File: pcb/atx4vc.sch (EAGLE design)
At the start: 38 parts, among them IC1 MY_7905DT, J2 ATX24RH

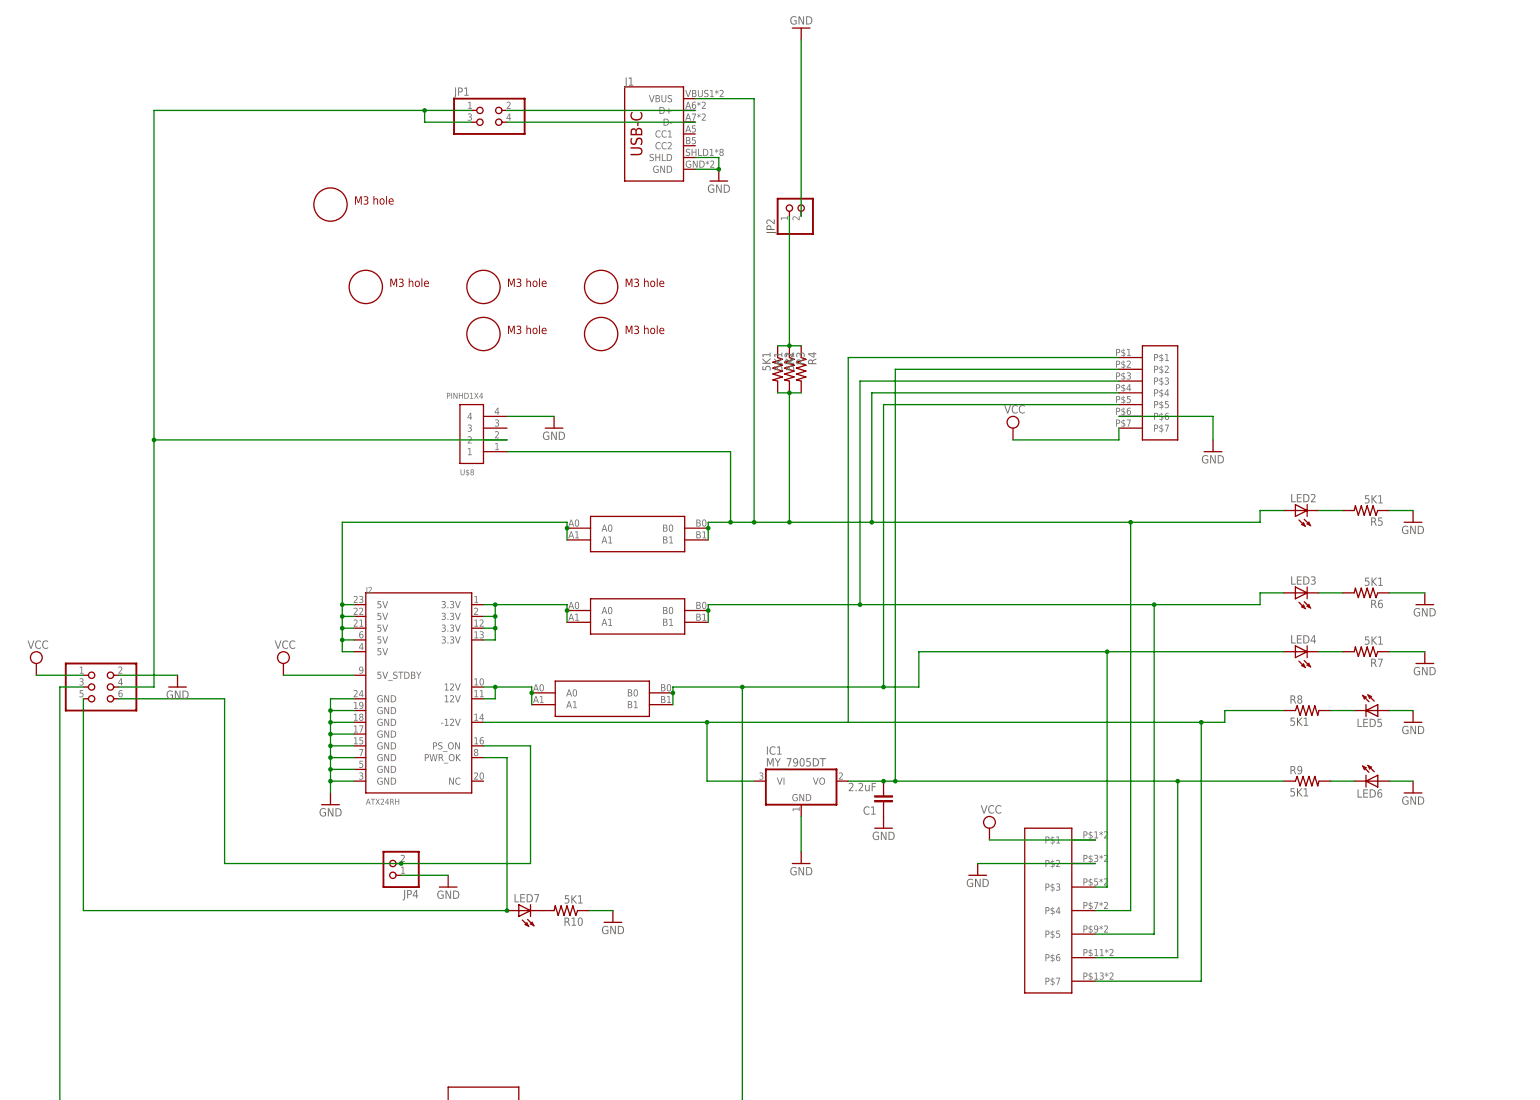
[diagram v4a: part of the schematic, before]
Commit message: added PG on terminal block, moved things around
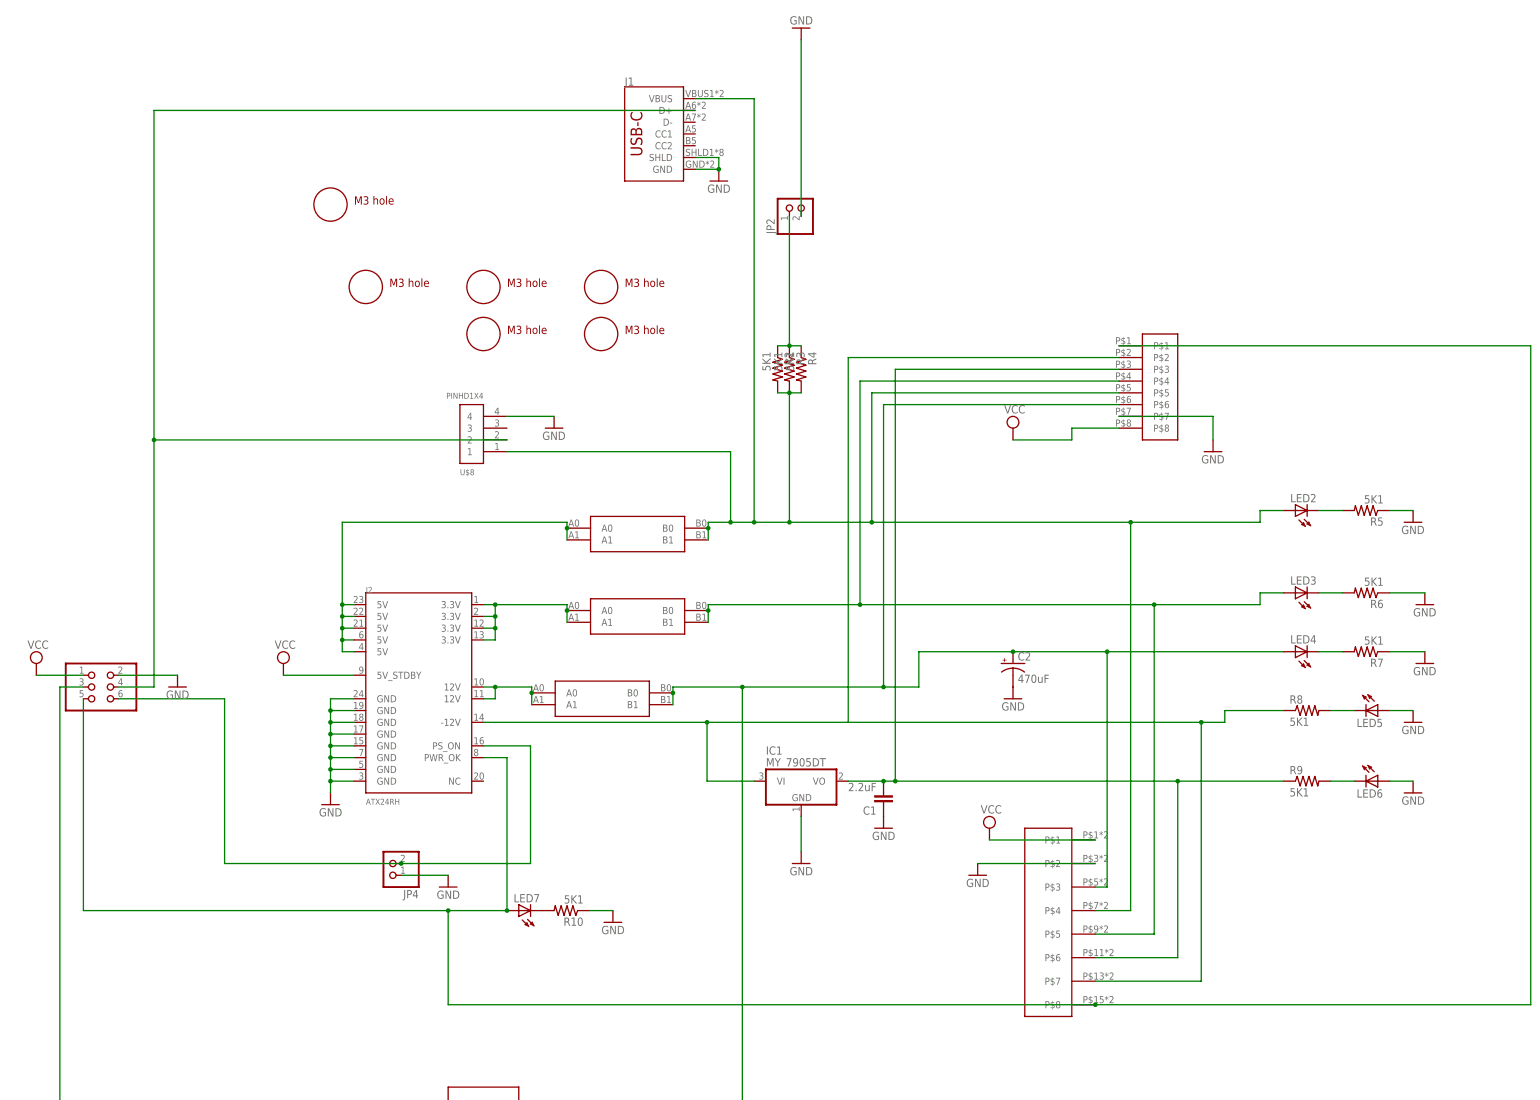
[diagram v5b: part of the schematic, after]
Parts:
- removed JP1: (no value), pinhead:PINHD-2X2
- added C2: 470uF, rcl:CPOL-USSMCD
- U$12: value DG2204R-5.0 -> DG2204R-5.0-8DG2204-8; device atx4vc:DG2204R-5.0 -> atx4vc:DG2204R-5.0-8DG2204-8
- U$7: value VH396 -> VH396_8P; device 396_conn:VH396 -> 396_conn:VH396_8P
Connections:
- removed net N$4: J1.D+, JP1.2
- removed net N$6: J1.D-, JP1.4
- net -12V: now also U$7.P$2; no longer U$7.P$1
- net -5V: now also U$7.P$3; no longer U$7.P$2
- net F12V: now also C2.+, U$7.P$6; no longer U$7.P$5
- net F3V3: now also U$7.P$4; no longer U$7.P$3
- net F5V: now also U$7.P$5; no longer U$7.P$4
- net GND: now also C2.-, U$7.P$7; no longer U$7.P$6
- net N$11: now also U$12.P$8, U$7.P$1
- net N$7: now also J1.D+; no longer JP1.1, JP1.3
- net VCC: now also U$7.P$8; no longer U$7.P$7

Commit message: adding more caps
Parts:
- added C10, C4, C5, C6, C7, C8, C9: 2.2uF, atx_power_control:CAP0805
- added C27: 47uF, clock:C-USC1210
- added C3: 470uF, rcl:CPOL-USSMCD
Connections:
- net -12V: now also C8.2
- net F12V: now also C6.2, C7.2
- net F3V3: now also C10.2, C27.1, C9.2
- net F5V: now also C3.+, C4.2, C5.2
- net GND: now also C10.1, C27.2, C3.-, C4.1, C5.1, C6.1, C7.1, C8.1, C9.1

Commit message: adding more caps
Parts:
- added C11: 47uF, clock:C-USC1210
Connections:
- net F12V: now also C11.1
- net GND: now also C11.2
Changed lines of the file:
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@@
 <part name="GND16" library="supply1" deviceset="GND" device=""/>
 <part name="GND22" library="supply1" deviceset="GND" device=""/>
+<part name="C11" library="clock" deviceset="C-US" device="C1210" value="47uF"/>
+<part name="GND23" library="supply1" deviceset="GND" device=""/>
 </parts>
 <sheets>
@@
 <instance part="GND22" gate="1" x="304.8" y="12.7" smashed="yes" rot="MR0">
 <attribute name="VALUE" x="307.34" y="10.16" size="1.778" layer="96" rot="MR0"/>
+</instance>
+<instance part="C11" gate="G$1" x="406.4" y="10.16" smashed="yes">
+<attribute name="NAME" x="407.416" y="10.795" size="1.778" layer="95"/>
+<attribute name="VALUE" x="407.416" y="5.969" size="1.778" layer="96"/>
+</instance>
+<instance part="GND23" gate="1" x="406.4" y="2.54" smashed="yes" rot="MR0">
+<attribute name="VALUE" x="408.94" y="0" size="1.778" layer="96" rot="MR0"/>
 </instance>
 </instances>
@@
 <pinref part="C9" gate="G$1" pin="1"/>
 <pinref part="GND22" gate="1" pin="GND"/>
+</segment>
+<segment>
+<pinref part="C11" gate="G$1" pin="2"/>
+<pinref part="GND23" gate="1" pin="GND"/>
 </segment>
 </net>
@@
 <wire x1="363.22" y1="12.7" x2="375.92" y2="12.7" width="0.1524" layer="91"/>
 <wire x1="375.92" y1="12.7" x2="383.54" y2="12.7" width="0.1524" layer="91"/>
-<wire x1="383.54" y1="12.7" x2="421.64" y2="12.7" width="0.1524" layer="91"/>
+<wire x1="383.54" y1="12.7" x2="406.4" y2="12.7" width="0.1524" layer="91"/>
+<wire x1="406.4" y1="12.7" x2="421.64" y2="12.7" width="0.1524" layer="91"/>
 <wire x1="304.8" y1="5.08" x2="304.8" y2="-96.52" width="0.1524" layer="91"/>
 <junction x="304.8" y="5.08"/>
@@
 <pinref part="C7" gate="G$1" pin="2"/>
 <junction x="375.92" y="12.7"/>
-</segment>
-</net>
+<pinref part="C11" gate="G$1" pin="1"/>
+<junction x="406.4" y="12.7"/>
+</segment>
+</net>

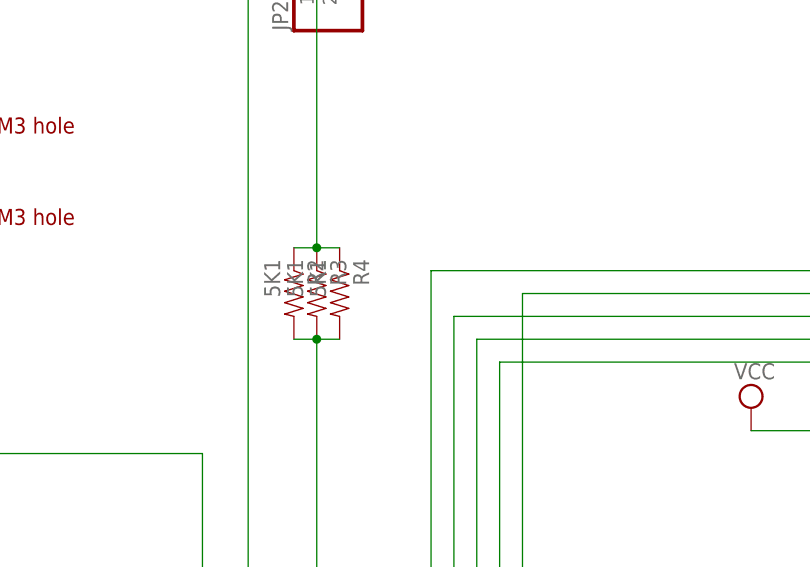
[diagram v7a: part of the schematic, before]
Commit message: added power LED resistor bypass
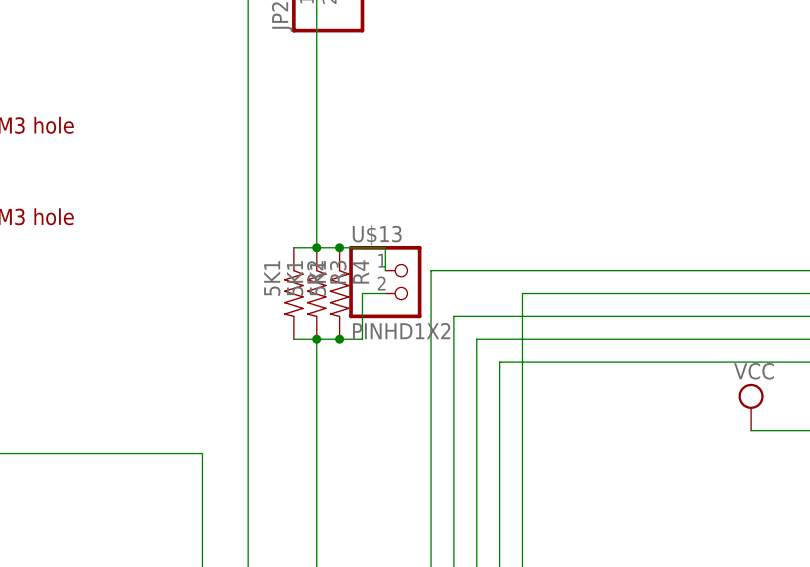
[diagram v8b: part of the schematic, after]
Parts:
- added U$13: PINHD1X2, adafruit_changed:PINHD1X2
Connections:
- net F5V: now also U$13.2
- net N$17: now also U$13.1
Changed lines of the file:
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@@
 <part name="C11" library="clock" deviceset="C-US" device="C1210" value="47uF"/>
 <part name="GND23" library="supply1" deviceset="GND" device=""/>
+<part name="U$13" library="adafruit_changed" deviceset="PINHD1X2" device=""/>
 </parts>
 <sheets>
@@
 <instance part="GND23" gate="1" x="406.4" y="2.54" smashed="yes" rot="MR0">
 <attribute name="VALUE" x="408.94" y="0" size="1.778" layer="96" rot="MR0"/>
+</instance>
+<instance part="U$13" gate="1" x="325.12" y="73.66" smashed="yes">
+<attribute name="NAME" x="318.77" y="79.375" size="1.778" layer="95"/>
+<attribute name="VALUE" x="318.77" y="68.58" size="1.778" layer="96"/>
 </instance>
 </instances>
@@
 <pinref part="C5" gate="G$1" pin="2"/>
 <junction x="383.54" y="40.64"/>
+<pinref part="U$13" gate="1" pin="2"/>
+<wire x1="322.58" y1="73.66" x2="320.04" y2="73.66" width="0.1524" layer="91"/>
+<wire x1="320.04" y1="73.66" x2="320.04" y2="68.58" width="0.1524" layer="91"/>
+<wire x1="320.04" y1="68.58" x2="317.5" y2="68.58" width="0.1524" layer="91"/>
+<junction x="317.5" y="68.58"/>
 </segment>
 </net>
@@
 <pinref part="R2" gate="G$1" pin="1"/>
 <wire x1="314.96" y1="78.74" x2="312.42" y2="78.74" width="0.1524" layer="91"/>
-</segment>
-</net>
+<pinref part="U$13" gate="1" pin="1"/>
+<wire x1="322.58" y1="76.2" x2="322.58" y2="78.74" width="0.1524" layer="91"/>
+<wire x1="322.58" y1="78.74" x2="317.5" y2="78.74" width="0.1524" layer="91"/>
+<junction x="317.5" y="78.74"/>
+</segment>
+</net>
